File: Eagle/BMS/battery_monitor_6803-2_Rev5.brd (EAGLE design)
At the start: 65.8 x 53.3 mm, 68 parts, among them IC1 MIC2954-03WS, Q1 MOSFET-PCHANNELIRLML2244, Q10 IRF9530, Q2 MOSFET-NCHANNELBSS138, Q3 MOSFET-PCHANNELIRLML2244, Q4 MOSFET-PCHANNELIRLML2244, Q5 MOSFET-PCHANNELIRLML2244, Q6 MOSFET-NCHANNELBSS138, Q7 MOSFET-NCHANNELBSS138, Q8 MOSFET-NCHANNELBSS138, Q9 PMOS_AO4435

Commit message: Added voltage regulator to charging circuit of BMS.
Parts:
- removed A0: (no value), SparkFun:SJ_3
- removed U$7: TACTILE-SWITCH-7914G, GeekAmmo:7914G
- removed U$8: ARDUINO_R3_SHIELD, SparkFun-Boards:UNO_R3_SHIELD
- added A4: (no value), SparkFun:SJ_3
- added D3: SMD26PL-TP, SparkFun-DiscreteSemi:SOD-123
- added X1: W237-07P, con-wago-508:W237-7P
- C1: value 0.1uF -> 1uF
- C4: value 1uF -> 0.1uF
- R11: value 100k -> 4.7k
- R12: value 4.7k -> 100k
- R15, R20: value 4.7k -> 470
- R17, R18: value 470 -> 4.7k
- R21: value 4.7k -> 1Meg
- R24: value 1Meg -> 4.7k
- R3: value 3.3k -> 100
- R4: value 100 -> 3.3k
- U$3: value RESISTOR-POWER-3W -> TACTILE-SWITCH-7914G; device isaac1:RESISTOR-3W -> GeekAmmo:7914G
- U$4: value SCREW_TERMINAL_4 -> RESISTOR-POWER-3W; device isaac1:SCREW_TERMINAL_4 -> isaac1:RESISTOR-3W
- U$5: value LTC6803-2 -> ARDUINO_R3_SHIELD; device isaac1:FSOP-44 -> SparkFun-Boards:UNO_R3_SHIELD
- U$6: value SCREW_TERMINAL_2 -> LTC6803-2; device Isaac:SCREW_TERMINAL_2 -> isaac1:FSOP-44
- moved U$4 57.6 mm to (54.6, 36.7), turned to 90 degrees
- moved U$3 49.9 mm to (6.35, 49.4)
- moved U$5 44.1 mm to (67.3, 0.76), turned to 90 degrees
- moved R18 34.4 mm to (25.9, 6.10)
- moved U$6 31.0 mm to (34.3, 30.0), turned to 180 degrees
- moved R20 29.4 mm to (58.2, 18.0)
- moved Q4 29.3 mm to (27.8, 15.9), turned to 0 degrees
- moved D2 27.4 mm to (9.91, 42.4)
- moved R12 27.1 mm to (25.9, 32.5), turned to 0 degrees
- moved Q1 25.8 mm to (39.4, 39.0), turned to 270 degrees
- moved C6 24.8 mm to (11.3, 32.0), turned to 270 degrees
- moved R11 23.8 mm to (38.7, 12.4), turned to 180 degrees
- moved R24 18.1 mm to (45.7, 7.75), turned to 270 degrees
- moved R13 16.1 mm to (54.6, 9.65), turned to 90 degrees
- moved C1 15.9 mm to (41.1, 27.9), turned to 90 degrees
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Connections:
- removed net 5VREG: IC1.3, Q10.S, R26.2
- removed net NONE: D2.C, U$4.P$4
- removed net VIN: D2.A, Q10.D, U$8.VIN
- new net 12VREG: D2.A, IC1.3, U$5.VIN
- new net 12VUNREG: D3.A, IC1.1, Q10.D
- new net N$26: D3.C, X1.5
- new net WIRE: D2.C, X1.4
- net +5: now also R13.2, R17.2, R21.1, R24.2, U$5.5V; no longer R14.2, R15.2, R21.2, R24.1, U$8.5V
- net ALL_SYSTEMS_GO: now also Q2.1, R11.2, U$5.D8; no longer Q6.1, R13.2, U$8.D8
- net BATTERY+: now also Q10.S, R26.2, X1.1; no longer IC1.1, U$4.P$1
- net CHARGE: now also R14.2, U$5.D9; no longer R12.2, U$8.D9
- net CHARGER_CONNECTED: now also R19.2, U$5.D7; no longer R20.2, U$8.D7
- net CHARGER_IN: now also R18.2, X1.3; no longer R19.2, U$4.P$3
- net ESTOP1: now also U$3.3, U$3.4, X1.6; no longer U$6.P$1, U$7.3, U$7.4
- net ESTOP2: now also Q2.3, X1.7; no longer Q6.3, U$6.P$2
- net GND: now also A4.3, C1.1, C7.2, DZ3.2, R11.1, R14.1, R18.1, U$3.1, U$3.2, U$5.GND@0, U$5.GND@1, U$5.GND@2, U$6.26, X1.2; no longer A0.3, C1.2, C7.1, DZ1.2, R12.1, R13.1, R20.1, U$4.P$2, U$5.26, U$7.1, U$7.2, U$8.GND@0, U$8.GND@1, U$8.GND@2
- net MISO: now also R24.1, U$5.D12, U$6.43; no longer R21.1, U$5.43, U$8.D12
- net MOSI: now also U$5.D11, U$6.42; no longer U$5.42, U$8.D11
- net N$10: now also Q3.3, R16.2; no longer Q4.3, R17.2
- net N$11: now also Q3.1; no longer Q4.1
- net N$12: now also R20.2, U$4.P$1; no longer R18.2, U$3.P$1
- net N$13: now also R15.1; no longer R16.1
- net N$14: now also C2.1, DZ1.1, R7.2, U$6.20; no longer C1.1, DZ3.1, R6.2, U$5.20
- net N$15: now also C4.1, DZ3.1, R6.2, U$6.24; no longer C3.1, DZ1.1, R4.2, U$5.24
- net N$16: now also C3.1, DZ1.2, R3.2, U$6.22; no longer C2.1, DZ3.2, R5.2, U$5.22
- net N$17: now also R5.2, U$6.10, U$6.12, U$6.14, U$6.16, U$6.18, U$6.2, U$6.4, U$6.6, U$6.8; no longer R7.2, U$5.10, U$5.12, U$5.14, U$5.16, U$5.18, U$5.2, U$5.4, U$5.6, U$5.8
- net N$18: now also Q4.3; no longer Q1.3
- net N$19: now also C1.2, Q4.2, U$6.1; no longer C5.2, Q1.2, U$5.1
- net N$2: now also Q1.2, R6.1; no longer Q3.2, R4.1
- net N$20: now also Q4.1, Q6.3; no longer Q1.1, Q2.3
- net N$21: now also C6.2, R12.1, U$6.28; no longer C7.2, R11.1, U$5.28
- net N$22: now also R16.1; no longer R17.1
- net N$23: now also R20.1; no longer R18.1
- net N$24: now also R21.2, U$6.36; no longer R22.2, U$5.36
- net N$25: now also U$6.35; no longer U$5.35
- net N$27: now also R22.2, U$6.34; no longer R24.2, U$5.34
- net N$28: now also A2.2, U$6.40; no longer A3.2, U$5.40
- net N$29: now also R4.1; no longer R3.1
- net N$3: now also Q3.2, R3.1, U$4.P$2; no longer Q4.2, R5.1, U$3.P$2
- net N$30: now also A4.2, U$6.39; no longer A2.2, U$5.39
- net N$31: now also U$6.38; no longer U$5.38
- net N$32: now also A3.2, U$6.37; no longer A0.2, U$5.37
- net N$33: now also U$6.32; no longer U$5.32
- net N$34: now also C5.2, U$6.30; no longer C6.2, U$5.30
- net N$4: now also R5.1; no longer R6.1
- net N$5: now also Q1.3, R15.2; no longer Q3.3, R16.2
- net N$6: now also U$6.23; no longer U$5.23
- net N$7: now also Q1.1; no longer Q3.1
- net N$8: now also U$6.25; no longer U$5.25
- net N$9: now also R4.2, U$6.21; no longer R3.2, U$5.21
- net PWR: now also Q6.1, U$5.D6; no longer Q2.1, U$8.D6
- net SCK: now also U$5.D13, U$6.41; no longer U$5.41, U$8.D13
- net SCL: now also R17.1, U$5.SCL; no longer R15.1, U$8.SCL
- net SDA: now also R13.1, U$5.SDA; no longer R14.1, U$8.SDA
- net SS: now also U$5.D10, U$6.44; no longer U$5.44, U$8.D10
- net VREG: now also A4.1, C7.1, R12.2, U$6.31; no longer A0.1, C4.1, R11.2, U$5.31
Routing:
- net VIN: track 64.8 -> 0.00 mm
- net 12VUNREG: track 0.00 -> 38.8 mm
- net 12VREG: track 0.00 -> 36.4 mm, vias 0 -> 1
- net WIRE: track 0.00 -> 27.8 mm, vias 0 -> 1
- net CHARGER_IN: track 63.9 -> 87.0 mm
- net N$26: track 0.00 -> 22.7 mm, vias 0 -> 1
- net ESTOP1: track 50.7 -> 70.7 mm, vias 2 -> 0
- net NONE: track 11.8 -> 0.00 mm, vias 1 -> 0
- net 5VREG: track 11.0 -> 0.00 mm
- net N$15: track 41.7 -> 35.5 mm
- net ESTOP2: track 31.9 -> 35.3 mm
- net N$21: track 31.6 -> 28.3 mm, vias 1 -> 2
- net N$3: track 84.1 -> 80.9 mm
- net N$2: track 83.4 -> 80.3 mm
- net N$14: track 30.6 -> 27.8 mm
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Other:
- board size 65.8 x 53.3 mm -> 69.1 x 53.3 mm
- board text added: "12Vo REG"
- board text added: "12Vo UNREG"
- board text added: "ITEST BMS Rev 5"
- board text removed: "ITEST BMS Rev 3"
- board text removed: "VOUT"

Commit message: Changed linear regulator device.
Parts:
- IC1: value MIC2954-03WS -> MIC2920A-12WS
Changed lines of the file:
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@@
 <attribute name="NAME" x="17.145" y="19.304" size="0.4064" layer="25"/>
 </element>
-<element name="IC1" library="linear" package="SOT223" value="MIC2954-03WS" x="4.826" y="42.545" smashed="yes">
+<element name="IC1" library="linear" package="SOT223" value="MIC2920A-12WS" x="4.826" y="42.545" smashed="yes">
 <attribute name="NAME" x="2.286" y="42.5958" size="1.27" layer="25"/>
 </element>

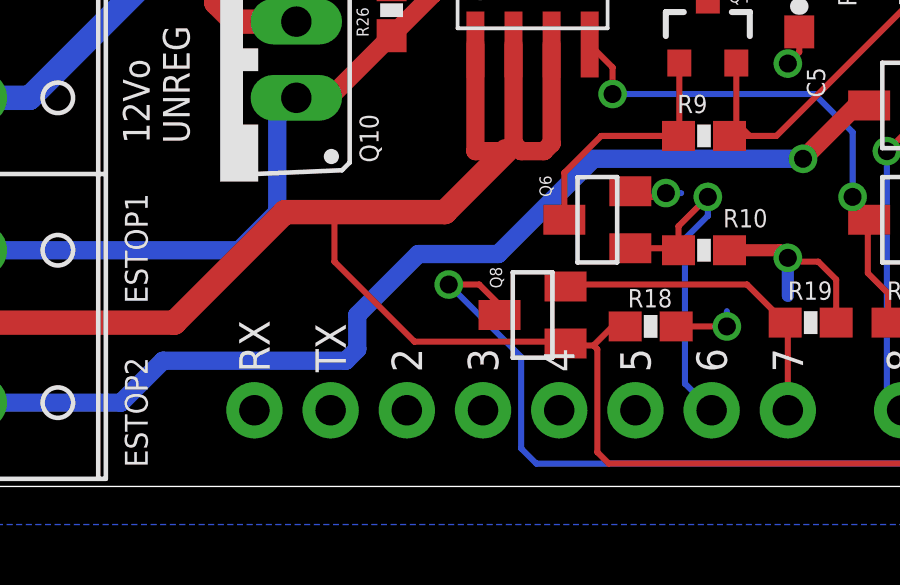
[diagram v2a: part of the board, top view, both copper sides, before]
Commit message: Fixed error with charging line shorting to +5V
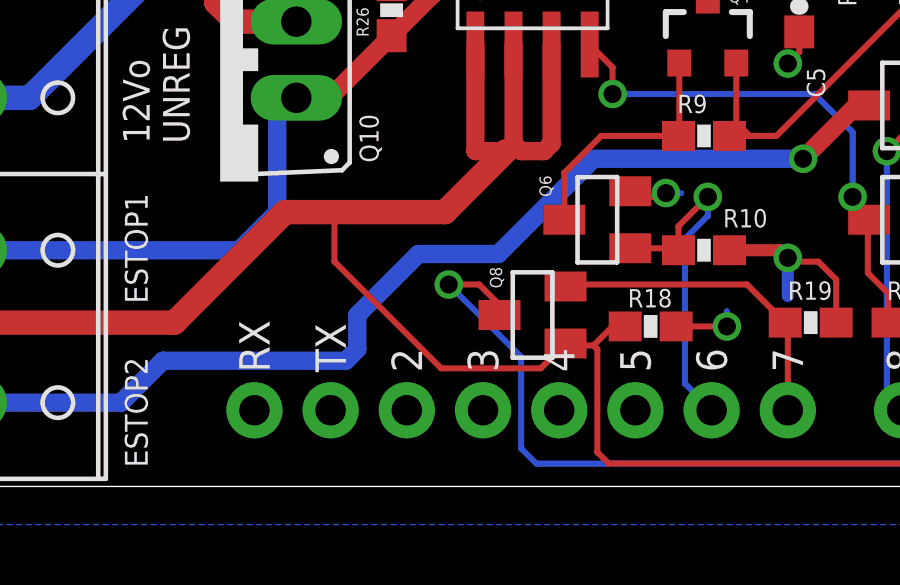
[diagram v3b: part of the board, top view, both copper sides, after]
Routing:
- net CHARGER_IN: track 87.0 -> 87.8 mm
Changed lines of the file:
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@@
 <?xml version="1.0" encoding="utf-8"?>
 <!DOCTYPE eagle SYSTEM "eagle.dtd">
-<eagle version="7.3.0">
+<eagle version="7.4.0">
 <drawing>
 <settings>
@@
 <wire x1="21.59" y1="11.938" x2="21.336" y2="12.192" width="0.6096" layer="1"/>
 <wire x1="23.071" y1="5.527" x2="23.01" y2="5.588" width="0.2032" layer="1"/>
-<wire x1="23.01" y1="5.588" x2="18.034" y2="5.588" width="0.2032" layer="1"/>
-<wire x1="18.034" y1="5.588" x2="15.367" y2="8.255" width="0.2032" layer="1"/>
+<wire x1="18.923" y1="4.699" x2="15.367" y2="8.255" width="0.2032" layer="1"/>
 <wire x1="15.367" y1="8.255" x2="15.367" y2="9.906" width="0.2032" layer="1"/>
 <wire x1="15.367" y1="9.906" x2="19.05" y2="9.906" width="0.8128" layer="1"/>
@@
 <wire x1="-0.254" y1="7.874" x2="-0.254" y2="20.955" width="0.8128" layer="1"/>
 <wire x1="-0.254" y1="20.955" x2="2.667" y2="23.876" width="0.8128" layer="1"/>
+<wire x1="18.923" y1="4.699" x2="22.243" y2="4.699" width="0.2032" layer="1"/>
+<wire x1="22.243" y1="4.699" x2="23.071" y2="5.527" width="0.2032" layer="1"/>
 </signal>
 <signal name="N$24">
